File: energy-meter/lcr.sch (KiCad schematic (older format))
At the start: 42 parts, among them U10 MCP6V96T-E/OT, U11 TS5A3159ADBVR, U12 MCP6V96T-E/OT, U2 MCP6V96T-E/OT, U3 TS5A3159ADBVR, U7 LP2951-3.3_SOIC, U8 TS5A3159ADBVR

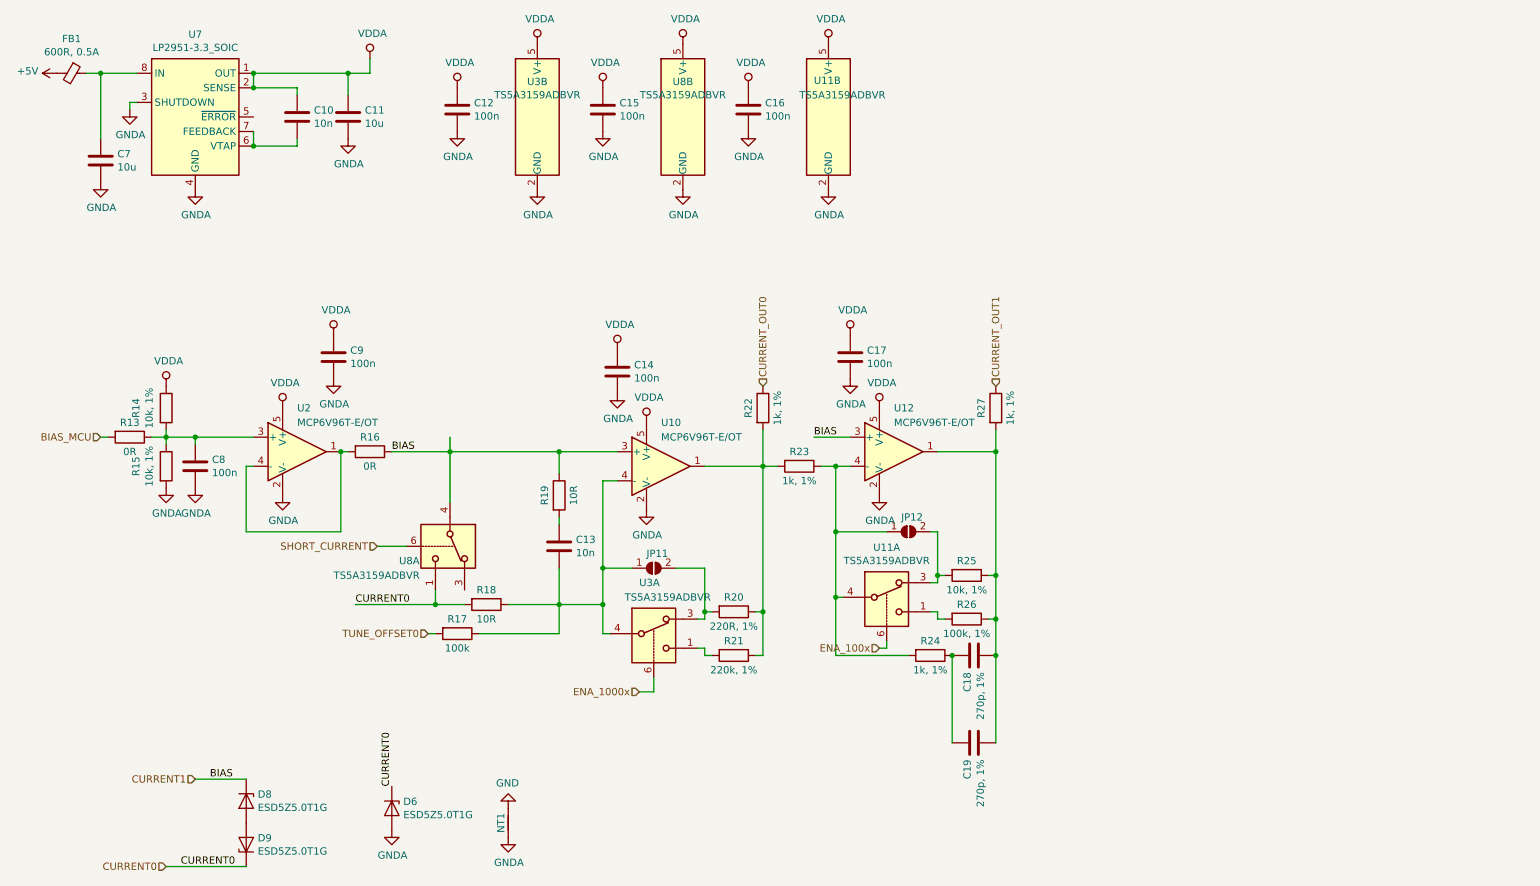
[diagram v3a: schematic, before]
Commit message: handle most TODOs in schematic, PCB to be done
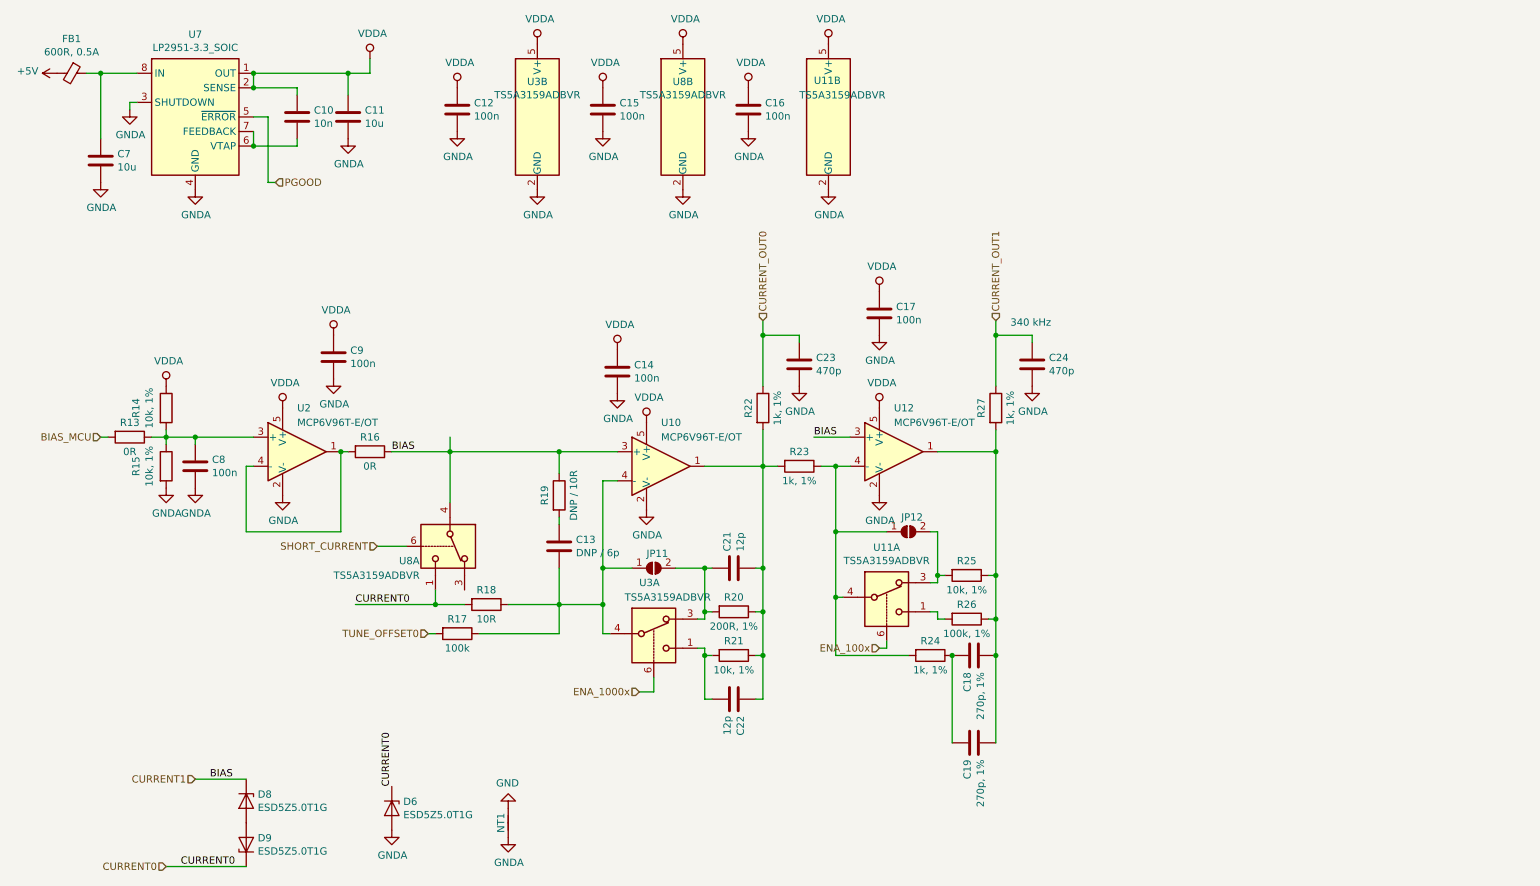
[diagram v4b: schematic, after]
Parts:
- added C21, C22: 12p, Capacitor_SMD:C_0603_1608Metric_Pad1.05x0.95mm_HandSolder, symbol Device:C
- added C23, C24: 470p, Capacitor_SMD:C_0603_1608Metric_Pad1.05x0.95mm_HandSolder, symbol Device:C
- C13: value 10n -> DNP / 6p
- R19: value 10R -> DNP / 10R
- R20: value 220R, 1% -> 200R, 1%
- R21: value 220k, 1% -> 10k, 1%
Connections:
- net CURRENT_OUT0: now also C23.1
- net CURRENT_OUT1: now also C24.1
- net GNDA: now also C23.2, C24.2
- net at R21.2, U3.1: now also C22.2
- net at JP11.2 (B), R20.2, U3.3: now also C21.1
- net PGOOD: now reaches U7.5 (~ERROR)
- net at R20.1, R21.1, R22.2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: now also C21.2, C22.1
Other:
- note added: "340 kHz"
- moved on the sheet: C17
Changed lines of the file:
@@
 $Descr A4 11693 8268
 encoding utf-8
-Sheet 2 4
+Sheet 4 4
 Title ""
 Date ""
@@
 AR Path="/607B74C2/6124611C" Ref="R20"  Part="1"
 F 0 "R20" V 5450 4700 50  0000 C CNN
-F 1 "220R, 1%" V 5650 4700 50  0000 C CNN
+F 1 "200R, 1%" V 5650 4700 50  0000 C CNN
 F 2 "Resistor_SMD:R_0603_1608Metric_Pad1.05x0.95mm_HandSolder" V 5480 4700 50  0001 C CNN
 F 3 "~" H 5550 4700 50  0001 C CNN
@@
 AR Path="/607B74C2/6124648D" Ref="R21"  Part="1"
 F 0 "R21" V 5450 5000 50  0000 C CNN
-F 1 "220k, 1%" V 5650 5000 50  0000 C CNN
+F 1 "10k, 1%" V 5650 5000 50  0000 C CNN
 F 2 "Resistor_SMD:R_0603_1608Metric_Pad1.05x0.95mm_HandSolder" V 5480 5000 50  0001 C CNN
 F 3 "~" H 5550 5000 50  0001 C CNN
@@
 	5750 3700 5350 3700
 Connection ~ 5750 4700
-Text HLabel 5750 3150 1    50   Input ~ 0
+Text HLabel 5750 2700 1    50   Input ~ 0
 CURRENT_OUT0
 Wire Wire Line
@@
 	5000 5250 5000 5150
 Wire Wire Line
-	5750 3700 5750 4700
+	5750 3700 5750 4400
 Connection ~ 5750 3700
 Wire Wire Line
@@
 AR Path="/607B74C2/612D8714" Ref="R19"  Part="1"
 F 0 "R19" V 4250 3900 50  0000 C CNN
-F 1 "10R" V 4450 3900 50  0000 C CNN
+F 1 "DNP / 10R" V 4450 3900 50  0000 C CNN
 F 2 "Resistor_SMD:R_0603_1608Metric_Pad1.05x0.95mm_HandSolder" V 4280 3900 50  0001 C CNN
 F 3 "~" H 4350 3900 50  0001 C CNN
@@
 AR Path="/607B74C2/612D8DA6" Ref="C13"  Part="1"
 F 0 "C13" H 4465 4296 50  0000 L CNN
-F 1 "10n" H 4465 4205 50  0000 L CNN
+F 1 "DNP / 6p" H 4465 4205 50  0000 L CNN
 F 2 "Capacitor_SMD:C_0603_1608Metric_Pad1.05x0.95mm_HandSolder" H 4388 4100 50  0001 C CNN
 F 3 "~" H 4350 4250 50  0001 C CNN
@@
 L Device:C C?
 U 1 1 6136EEA1
-P 6350 2950
+P 6550 2650
 AR Path="/602A2F7F/6136EEA1" Ref="C?"  Part="1"
 AR Path="/602A3FC4/6136EEA1" Ref="C?"  Part="1"
 AR Path="/60514CC5/6136EEA1" Ref="C?"  Part="1"
 AR Path="/607B74C2/6136EEA1" Ref="C17"  Part="1"
-F 0 "C17" H 6465 2996 50  0000 L CNN
-F 1 "100n" H 6465 2905 50  0000 L CNN
-F 2 "Capacitor_SMD:C_0603_1608Metric_Pad1.05x0.95mm_HandSolder" H 6388 2800 50  0001 C CNN
-F 3 "~" H 6350 2950 50  0001 C CNN
-	1    6350 2950
+F 0 "C17" H 6665 2696 50  0000 L CNN
+F 1 "100n" H 6665 2605 50  0000 L CNN
+F 2 "Capacitor_SMD:C_0603_1608Metric_Pad1.05x0.95mm_HandSolder" H 6588 2500 50  0001 C CNN
+F 3 "~" H 6550 2650 50  0001 C CNN
+	1    6550 2650
 	1    0    0    -1
 $EndComp
@@
 L power:VDDA #PWR0160
 U 1 1 6136EEAB
-P 6350 2800
-F 0 "#PWR0160" H 6350 2650 50  0001 C CNN
-F 1 "VDDA" H 6367 2973 50  0000 C CNN
-F 2 "" H 6350 2800 50  0001 C CNN
-F 3 "" H 6350 2800 50  0001 C CNN
-	1    6350 2800
+P 6550 2500
+F 0 "#PWR0160" H 6550 2350 50  0001 C CNN
+F 1 "VDDA" H 6567 2673 50  0000 C CNN
+F 2 "" H 6550 2500 50  0001 C CNN
+F 3 "" H 6550 2500 50  0001 C CNN
+	1    6550 2500
 	1    0    0    -1
 $EndComp
@@
 L power:GNDA #PWR0161
 U 1 1 6136EEB5
-P 6350 3100
-F 0 "#PWR0161" H 6350 2850 50  0001 C CNN
-F 1 "GNDA" H 6355 2927 50  0000 C CNN
-F 2 "" H 6350 3100 50  0001 C CNN
-F 3 "" H 6350 3100 50  0001 C CNN
-	1    6350 3100
+P 6550 2800
+F 0 "#PWR0161" H 6550 2550 50  0001 C CNN
+F 1 "GNDA" H 6555 2627 50  0000 C CNN
+F 2 "" H 6550 2800 50  0001 C CNN
+F 3 "" H 6550 2800 50  0001 C CNN
+	1    6550 2800
 	1    0    0    -1
 $EndComp
@@
 	7350 3600 6950 3600
 Connection ~ 7350 4450
-Text HLabel 7350 3150 1    50   Input ~ 0
+Text HLabel 7350 2700 1    50   Input ~ 0
 CURRENT_OUT1
 Wire Wire Line
@@
 	1    0    0    -1
 $EndComp
+$Comp
+L Device:C C?
+U 1 1 60D2D848
+P 5550 5300
+AR Path="/602A2F7F/60D2D848" Ref="C?"  Part="1"
+AR Path="/602A3FC4/60D2D848" Ref="C?"  Part="1"
+AR Path="/60514CC5/60D2D848" Ref="C?"  Part="1"
+AR Path="/607B74C2/60D2D848" Ref="C22"  Part="1"
+F 0 "C22" H 5665 5346 50  0000 L CNN
+F 1 "12p" H 5665 5255 50  0000 L CNN
+F 2 "Capacitor_SMD:C_0603_1608Metric_Pad1.05x0.95mm_HandSolder" H 5588 5150 50  0001 C CNN
+F 3 "~" H 5550 5300 50  0001 C CNN
+	1    5550 5300
+	0    1    1    0
+$EndComp
+Wire Wire Line
+	5750 5000 5750 5300
+Wire Wire Line
+	5750 5300 5700 5300
+Connection ~ 5750 5000
+Wire Wire Line
+	5400 5300 5350 5300
+Wire Wire Line
+	5350 5300 5350 5000
+Connection ~ 5350 5000
+$Comp
+L Device:C C?
+U 1 1 60D3D16A
+P 5550 4400
+AR Path="/602A2F7F/60D3D16A" Ref="C?"  Part="1"
+AR Path="/602A3FC4/60D3D16A" Ref="C?"  Part="1"
+AR Path="/60514CC5/60D3D16A" Ref="C?"  Part="1"
+AR Path="/607B74C2/60D3D16A" Ref="C21"  Part="1"
+F 0 "C21" H 5665 4446 50  0000 L CNN
+F 1 "12p" H 5665 4355 50  0000 L CNN
+F 2 "Capacitor_SMD:C_0603_1608Metric_Pad1.05x0.95mm_HandSolder" H 5588 4250 50  0001 C CNN
+F 3 "~" H 5550 4400 50  0001 C CNN
+	1    5550 4400
+	0    -1   -1   0
+$EndComp
+Wire Wire Line
+	5700 4400 5750 4400
+Connection ~ 5750 4400
+Wire Wire Line
+	5750 4400 5750 4700
+Wire Wire Line
+	5400 4400 5350 4400
+Connection ~ 5350 4400
+$Comp
+L Device:C C?
+U 1 1 60D466AA
+P 6000 3000
+AR Path="/602A2F7F/60D466AA" Ref="C?"  Part="1"
+AR Path="/602A3FC4/60D466AA" Ref="C?"  Part="1"
+AR Path="/60514CC5/60D466AA" Ref="C?"  Part="1"
+AR Path="/607B74C2/60D466AA" Ref="C23"  Part="1"
+F 0 "C23" H 6115 3046 50  0000 L CNN
+F 1 "470p" H 6115 2955 50  0000 L CNN
+F 2 "Capacitor_SMD:C_0603_1608Metric_Pad1.05x0.95mm_HandSolder" H 6038 2850 50  0001 C CNN
+F 3 "~" H 6000 3000 50  0001 C CNN
+	1    6000 3000
+	1    0    0    -1
+$EndComp
+$Comp
+L power:GNDA #PWR0170
+U 1 1 60D46BA7
+P 6000 3150
+F 0 "#PWR0170" H 6000 2900 50  0001 C CNN
+F 1 "GNDA" H 6005 2977 50  0000 C CNN
+F 2 "" H 6000 3150 50  0001 C CNN
+F 3 "" H 6000 3150 50  0001 C CNN
+	1    6000 3150
+	1    0    0    -1
+$EndComp
+Wire Wire Line
+	5750 3150 5750 2800
+Wire Wire Line
+	5750 2800 6000 2800
+Wire Wire Line
+	6000 2800 6000 2850
+Wire Wire Line
+	5750 2800 5750 2700
+Connection ~ 5750 2800
+$Comp
+L Device:C C?
+U 1 1 60D50DC6
+P 7600 3000
+AR Path="/602A2F7F/60D50DC6" Ref="C?"  Part="1"
+AR Path="/602A3FC4/60D50DC6" Ref="C?"  Part="1"
+AR Path="/60514CC5/60D50DC6" Ref="C?"  Part="1"
+AR Path="/607B74C2/60D50DC6" Ref="C24"  Part="1"
+F 0 "C24" H 7715 3046 50  0000 L CNN
+F 1 "470p" H 7715 2955 50  0000 L CNN
+F 2 "Capacitor_SMD:C_0603_1608Metric_Pad1.05x0.95mm_HandSolder" H 7638 2850 50  0001 C CNN
+F 3 "~" H 7600 3000 50  0001 C CNN
+	1    7600 3000
+	1    0    0    -1
+$EndComp
+$Comp
+L power:GNDA #PWR0171
+U 1 1 60D50DD0
+P 7600 3150
+F 0 "#PWR0171" H 7600 2900 50  0001 C CNN
+F 1 "GNDA" H 7605 2977 50  0000 C CNN
+F 2 "" H 7600 3150 50  0001 C CNN
+F 3 "" H 7600 3150 50  0001 C CNN
+	1    7600 3150
+	1    0    0    -1
+$EndComp
+Wire Wire Line
+	7350 2800 7600 2800
+Wire Wire Line
+	7600 2800 7600 2850
+Wire Wire Line
+	7350 2800 7350 2700
+Wire Wire Line
+	7350 2800 7350 3150
+Connection ~ 7350 2800
+Text HLabel 2400 1750 2    50   Input ~ 0
+PGOOD
+Wire Wire Line
+	2250 1300 2350 1300
+Wire Wire Line
+	2350 1300 2350 1750
+Wire Wire Line
+	2350 1750 2400 1750
+Text Notes 7450 2750 0    50   ~ 0
+340 kHz
 $EndSCHEMATC

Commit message: old changes
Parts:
- added J5, J6: SMA, Connector_Coaxial:SMA_Samtec_SMA-J-P-H-ST-EM1_EdgeMount, symbol Connector:Conn_Coaxial
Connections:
- net CURRENT1: now also J5.2 (Ext), J6.2 (Ext)
- net CURRENT_OUT0: now also J5.1 (In)
- net CURRENT_OUT1: now also J6.1 (In)
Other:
- note added: "NOTE: SMA outer connector will be connected to the\noscilloscope's ground. Either the osci or the energy meter\nmust have a floating power supply.\n\nThe SMA for voltage is using a resistor divider (R3 and R4)\nwhich will be overridden by our BIAS (which is driven by\nan OpAmp). We usually don't do this because it may\nincrease noise."
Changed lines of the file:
@@
 Text Notes 7450 2750 0    50   ~ 0
 340 kHz
+$Comp
+L Connector:Conn_Coaxial J5
+U 1 1 60E3584F
+P 8650 1900
+F 0 "J5" H 8750 1875 50  0000 L CNN
+F 1 "SMA" H 8750 1784 50  0000 L CNN
+F 2 "Connector_Coaxial:SMA_Samtec_SMA-J-P-H-ST-EM1_EdgeMount" H 8650 1900 50  0001 C CNN
+F 3 "https://datasheet.lcsc.com/lcsc/2004161132_BAT-WIRELESS-BWSMA-KE-P001_C496550.pdf" H 8650 1900 50  0001 C CNN
+F 4 "C496550, C530661, (C1509221)" H 8650 1900 50  0001 C CNN "LCSC"
+	1    8650 1900
+	1    0    0    -1
+$EndComp
+$Comp
+L Connector:Conn_Coaxial J6
+U 1 1 60E3F131
+P 8650 2400
+F 0 "J6" H 8750 2282 50  0000 L CNN
+F 1 "SMA" H 8750 2373 50  0000 L CNN
+F 2 "Connector_Coaxial:SMA_Samtec_SMA-J-P-H-ST-EM1_EdgeMount" H 8650 2400 50  0001 C CNN
+F 3 "https://datasheet.lcsc.com/lcsc/2004161132_BAT-WIRELESS-BWSMA-KE-P001_C496550.pdf" H 8650 2400 50  0001 C CNN
+F 4 "C496550, C530661, (C1509221)" H 8650 2400 50  0001 C CNN "LCSC"
+	1    8650 2400
+	1    0    0    1
+$EndComp
+Wire Wire Line
+	8650 2200 8650 2150
+Wire Wire Line
+	8650 2150 8850 2150
+Connection ~ 8650 2150
+Wire Wire Line
+	8650 2150 8650 2100
+Text HLabel 8450 1900 0    50   Input ~ 0
+CURRENT_OUT0
+Text HLabel 8450 2400 0    50   Input ~ 0
+CURRENT_OUT1
+Text Label 8850 2150 0    50   ~ 0
+BIAS
+Text Notes 8200 3200 0    50   ~ 0
+NOTE: SMA outer connector will be connected to the\noscilloscope's ground. Either the osci or the energy meter\nmust have a floating power supply.\n\nThe SMA for voltage is using a resistor divider (R3 and R4)\nwhich will be overridden by our BIAS (which is driven by\nan OpAmp). We usually don't do this because it may\nincrease noise.
 $EndSCHEMATC
